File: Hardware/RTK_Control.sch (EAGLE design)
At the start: 294 parts, among them J3 MICRO-SD-PUSH-PUSH-EXT-PIN, J4 Vertical Qwiic Connector, J9 MAGJACK-POE, U1 ESP32-WROVER-IE, U10 POE_PSU-DP990X, U11 MCP6021T, U12 AP7361C-33, U13 MCP6021T, U14 BP2G1+_POWER_SPLITTER, U15 USB251XB, U16 SN74AVC4T774PW, U2 CH340C, U3 XC6222B331MR-G, U4 U-BLOX_ZED-F9P, U5 U-BLOX_NEO-D9S-00B, U6 XC6222B331MR-G, U7 W5500, U8 LARA-R6001, U9 74LVC4066D_QUAD_BILATERAL_SWI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, Y1 25MHz, Y2 24MHz

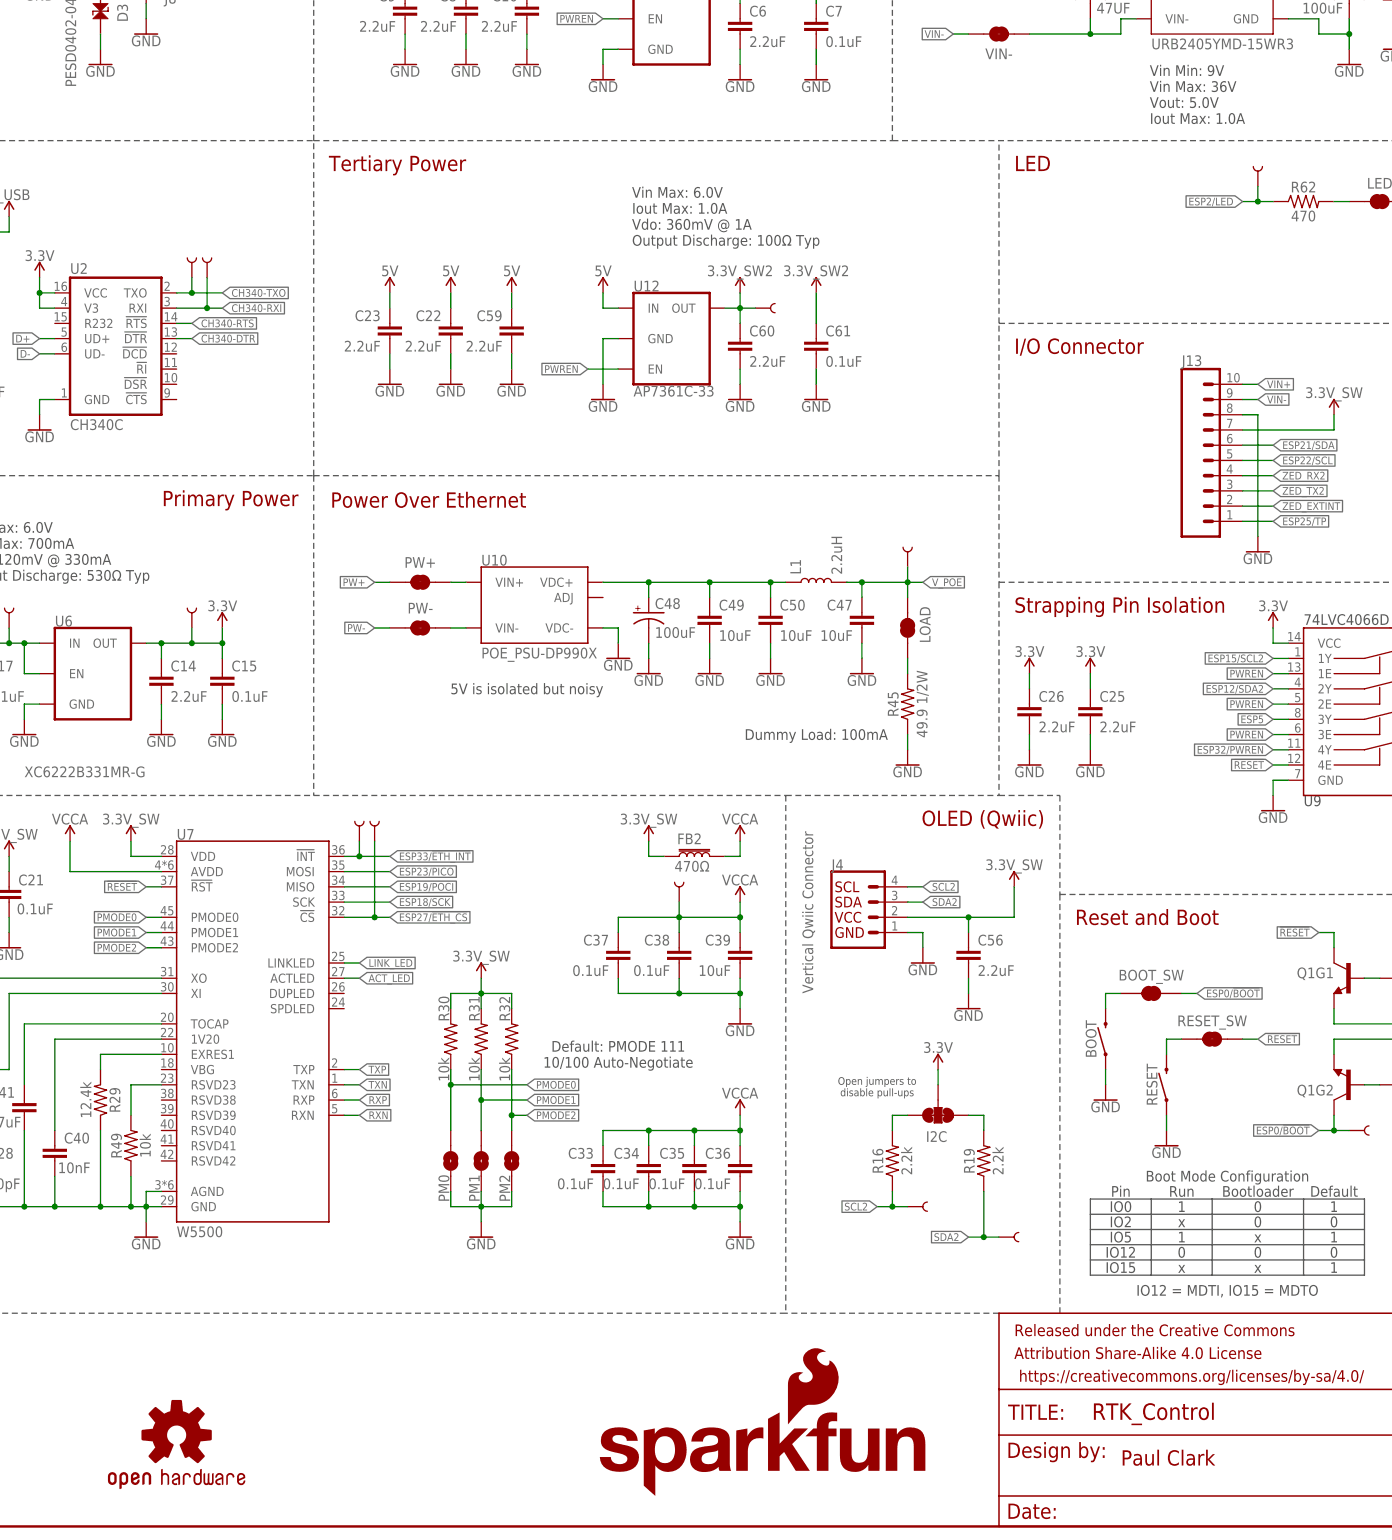
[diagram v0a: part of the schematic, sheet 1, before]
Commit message: Update DC-DC and PoE voltages and currents
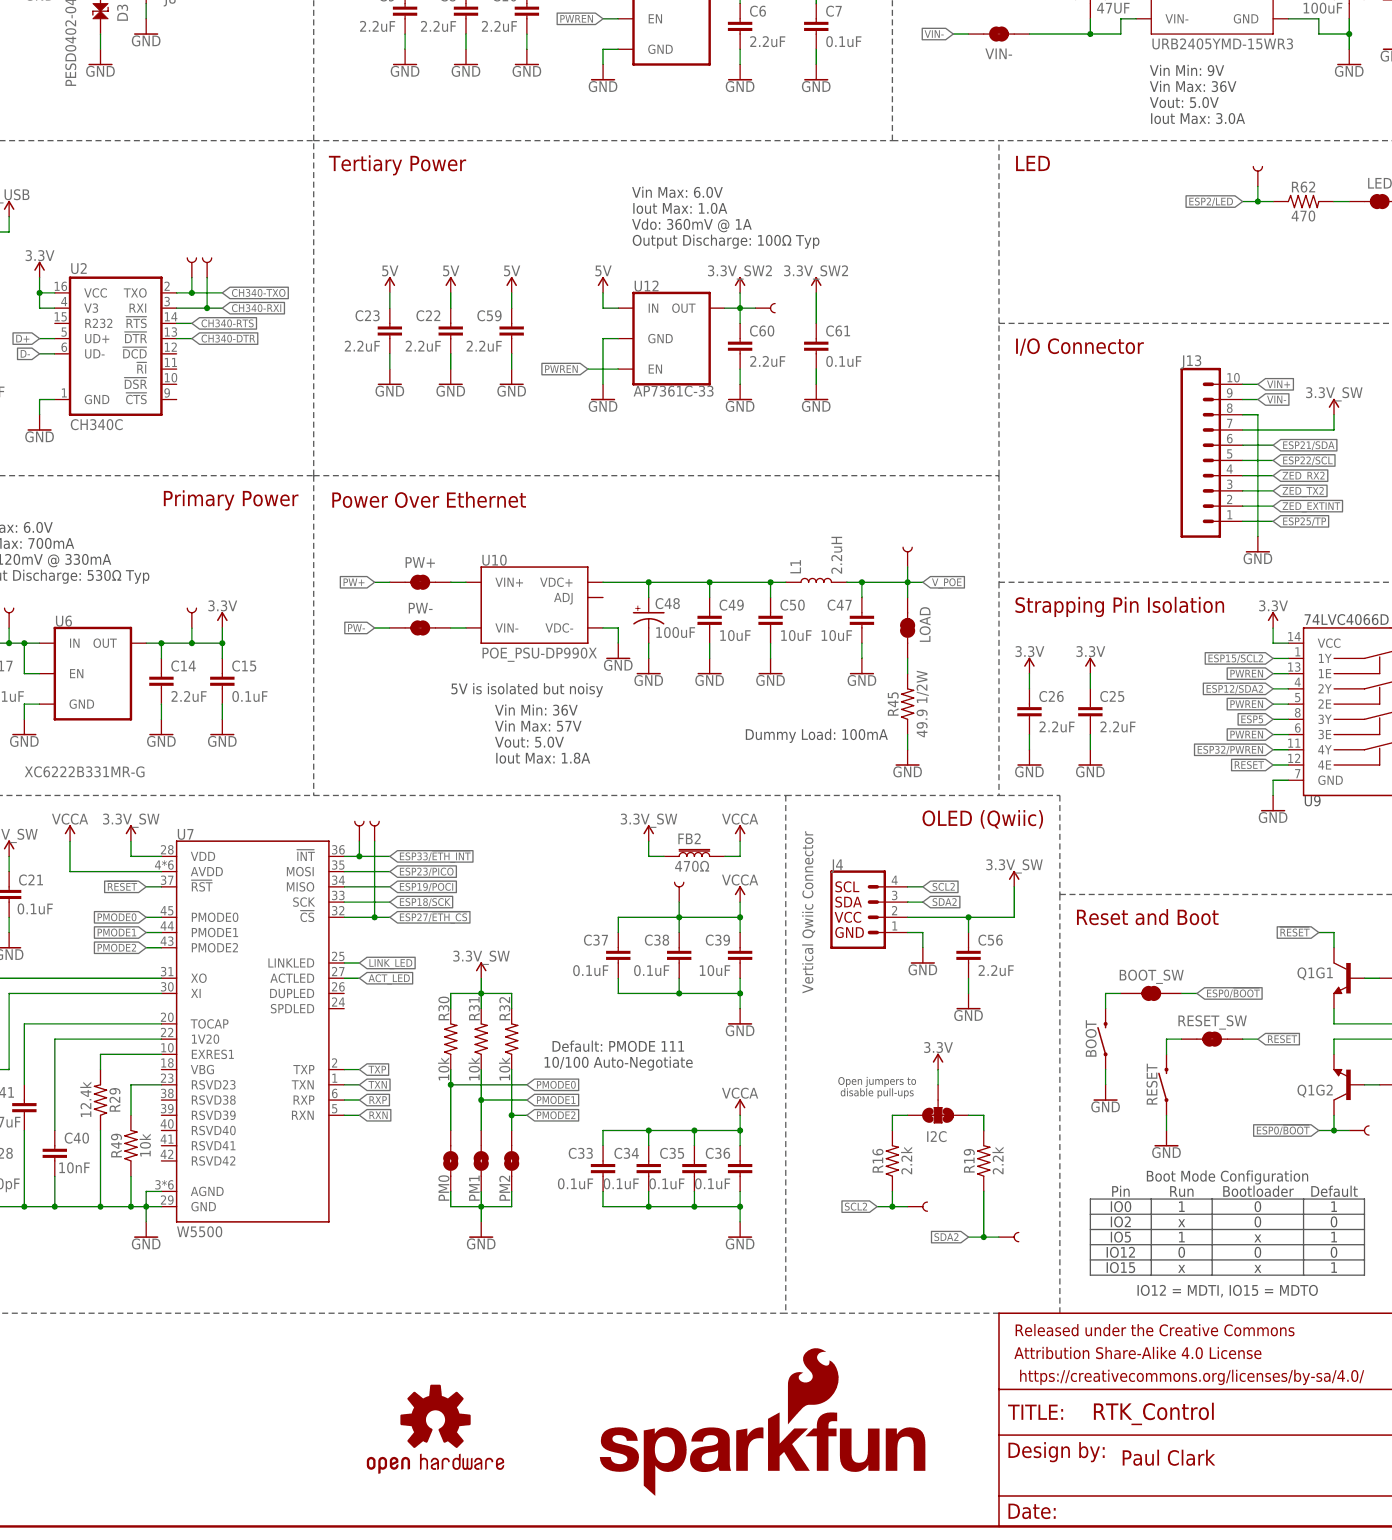
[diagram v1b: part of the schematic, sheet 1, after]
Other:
- note added: "Vin Min: 36V Vin Max: 57V Vout: 5.0V Iout Max: 1.8A"
- note added: "Vin Min: 9V Vin Max: 36V Vout: 5.0V Iout Max: 3.0A"
- note removed: "Vin Min: 9V Vin Max: 36V Vout: 5.0V Iout Max: 1.0A"
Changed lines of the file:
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@@
 Vin Max: 36V
 Vout: 5.0V
-Iout Max: 1.0A</text>
+Iout Max: 3.0A</text>
+<text x="246.126" y="127.254" size="1.778" layer="97" font="vector">Vin Min: 36V
+Vin Max: 57V
+Vout: 5.0V
+Iout Max: 1.8A</text>
 </plain>
 <instances>
@@
 <instance part="5V" gate="G$1" x="165.1" y="149.86" smashed="yes" rot="R90"/>
 <instance part="H4" gate="G$1" x="426.72" y="30.48" smashed="yes"/>
-<instance part="LOGO4" gate="G$1" x="193.04" y="15.24" smashed="yes"/>
+<instance part="LOGO4" gate="G$1" x="236.22" y="17.78" smashed="yes"/>
 <instance part="SUPPLY7" gate="G$1" x="165.1" y="218.44" smashed="yes">
 <attribute name="VALUE" x="165.1" y="221.234" size="1.778" layer="96" align="bottom-center"/>

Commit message: Updates after airwire review
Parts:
- removed R50, R51, R52: 10k, SparkFun-Resistors:10KOHM-0603-1/10W-1%
- added VID1: 10k, SparkFun-Resistors:10KOHM-0603-1/10W-1%
- added VID2: 1k, SparkFun-Resistors:1KOHM-0603-1/10W-1%
- D3: value PESD0402-0402 -> PESD0402
- renumbered U$73 to U17
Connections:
- net DET renamed ESP36/SD_DET
- removed net LARA_RXDO: U16.B2
- removed net LARA_TXDI: U16.B1
- removed net N$37: R50.2, R51.2, U1.IA35
- removed net N$39: R51.1, R52.2
- new net ESP35/VID: U1.IA35, VID1.2, VID2.2
- net 3.3V: now also VID2.1; no longer R52.1
- net ESP13/LARA_TXDI: now also U16.B1
- net ESP14/LARA_RXDO: now also U16.B2
- net GND: now also U16.B4, VID1.1; no longer R50.1
- net VCCIO: now also U16.DIR4
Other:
- note added: "Pin 35 floats at 0.18V approx. 3.3 / 13.3 = 0.82V (0.74 - 0.90) 10 / 30 = 1.1V (0.99 - 1.21) 10 / 20 = 1.65V (1.49 - 1.82) 20 / 30 = 2.2V (1.98 - 2.42) 10 / 13.3 = 2.48V (2.23 - 2.73) 10 / 11 = 3.00V (2.70 - 3.30)"
- note added: "Product Identifier"
- note added: "RTK Product Voltage IDs: Surveyor: Express: Reference Station: Facet: Facet L-Band: Express Plus: Control:"
- moved on the sheet: C11, C13, C18, C19, C20, D1, D3, ESP32_RF, FB1, GNSS_RF, J8, R11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

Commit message: Ready for routing
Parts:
- added ESP5: TEST-POINTPOGO_PTH, SparkFun-Connectors:TEST-POINTPOGO_PTH
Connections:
- new net N$37: ESP5.1, U9.3Z
- net D+_LARA: now also R10.1; no longer R9.1
- net D-_LARA: now also R9.1; no longer R10.1
- net GND: no longer U16.B4
- net VCCIO: now also U16.A4
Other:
- moved on the sheet: C19
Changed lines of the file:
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@@
 <part name="SDA" library="SparkFun-Connectors" deviceset="TEST-POINT" device="POGO_PTH" value="TEST-POINTPOGO_PTH"/>
 <part name="SUPPLY63" library="SparkFun-PowerSymbols" deviceset="3.3V_SW" device=""/>
+<part name="ESP5" library="SparkFun-Connectors" deviceset="TEST-POINT" device="POGO_PTH" value="TEST-POINTPOGO_PTH"/>
+<part name="GND49" library="SparkFun-PowerSymbols" deviceset="GND" device=""/>
 </parts>
 <sheets>
@@
 <attribute name="VALUE" x="20.32" y="152.146" size="1.778" layer="96" align="top-center"/>
 </instance>
-<instance part="C19" gate="G$1" x="7.62" y="137.16" smashed="yes">
-<attribute name="NAME" x="9.144" y="140.081" size="1.778" layer="95" font="vector"/>
-<attribute name="VALUE" x="9.144" y="135.001" size="1.778" layer="96" font="vector"/>
+<instance part="C19" gate="G$1" x="7.62" y="134.62" smashed="yes">
+<attribute name="NAME" x="9.144" y="137.541" size="1.778" layer="95" font="vector"/>
+<attribute name="VALUE" x="9.144" y="132.461" size="1.778" layer="96" font="vector"/>
 </instance>
 <instance part="GND38" gate="1" x="7.62" y="127" smashed="yes">
 <attribute name="VALUE" x="7.62" y="126.746" size="1.778" layer="96" align="top-center"/>
 </instance>
-<instance part="SUPPLY27" gate="G$1" x="7.62" y="144.78" smashed="yes">
-<attribute name="VALUE" x="7.62" y="147.574" size="1.778" layer="96" align="bottom-center"/>
+<instance part="SUPPLY27" gate="G$1" x="7.62" y="142.24" smashed="yes">
+<attribute name="VALUE" x="7.62" y="145.034" size="1.778" layer="96" align="bottom-center"/>
 </instance>
 <instance part="SUPPLY28" gate="G$1" x="7.62" y="167.64" smashed="yes">
@@
 <instance part="SD_CS" gate="G$1" x="55.88" y="152.4" smashed="yes" rot="R90"/>
 <instance part="SCK" gate="G$1" x="53.34" y="144.78" smashed="yes" rot="R90"/>
-<instance part="GND" gate="G$1" x="10.16" y="132.08" smashed="yes"/>
+<instance part="GND" gate="G$1" x="134.62" y="137.16" smashed="yes" rot="R90"/>
 <instance part="RESET_SW" gate="G$1" x="365.76" y="81.28" smashed="yes" rot="MR0">
 <attribute name="NAME" x="365.76" y="84.328" size="1.778" layer="95" font="vector" rot="MR0" align="center"/>
@@
 <attribute name="VALUE" x="355.6" y="246.38" size="1.778" layer="96" font="vector"/>
 </instance>
+<instance part="ESP5" gate="G$1" x="411.48" y="134.62" smashed="yes">
+<attribute name="NAME" x="416.56" y="134.62" size="1.778" layer="95" font="vector"/>
+</instance>
+<instance part="GND49" gate="1" x="134.62" y="132.08" smashed="yes">
+<attribute name="VALUE" x="134.62" y="131.826" size="1.778" layer="96" align="top-center"/>
+</instance>
 </instances>
 <busses>
@@
 <pinref part="C19" gate="G$1" pin="2"/>
 <wire x1="7.62" y1="129.54" x2="7.62" y2="132.08" width="0.1524" layer="91"/>
-<pinref part="GND" gate="G$1" pin="1"/>
-<wire x1="7.62" y1="132.08" x2="7.62" y2="134.62" width="0.1524" layer="91"/>
-<wire x1="10.16" y1="132.08" x2="7.62" y2="132.08" width="0.1524" layer="91"/>
-<junction x="7.62" y="132.08"/>
 </segment>
 <segment>
@@
 <wire x1="419.1" y1="248.92" x2="419.1" y2="251.46" width="0.1524" layer="91"/>
 </segment>
+<segment>
+<pinref part="GND49" gate="1" pin="GND"/>
+<pinref part="GND" gate="G$1" pin="1"/>
+<wire x1="134.62" y1="134.62" x2="134.62" y2="137.16" width="0.1524" layer="91"/>
+</segment>
 </net>
 <net name="3.3V" class="0">
@@
 <pinref part="C19" gate="G$1" pin="1"/>
 <pinref part="SUPPLY27" gate="G$1" pin="3.3V_SW"/>
-<wire x1="7.62" y1="142.24" x2="7.62" y2="144.78" width="0.1524" layer="91"/>
+<wire x1="7.62" y1="139.7" x2="7.62" y2="142.24" width="0.1524" layer="91"/>
 </segment>
 <segment>
@@
 </segment>
 </net>
+<net name="N$37" class="0">
+<segment>
+<pinref part="U9" gate="G$1" pin="3Z"/>
+<pinref part="ESP5" gate="G$1" pin="1"/>
+<wire x1="408.94" y1="134.62" x2="411.48" y2="134.62" width="0.1524" layer="91"/>
+</segment>
+</net>
 </nets>
 </sheet>
@@
 <wire x1="254" y1="157.48" x2="254" y2="279.4" width="0.1524" layer="97" style="longdash"/>
 <text x="326.39" y="187.96" size="1.778" layer="97" font="vector">90Ω</text>
-<text x="279.4" y="81.28" size="1.778" layer="97" align="center">7-bit unshifted I²C address: 0x2C</text>
+<text x="279.4" y="81.28" size="1.778" layer="97" font="vector" align="center">7-bit unshifted I²C address: 0x2C</text>
 <text x="279.4" y="76.2" size="1.27" layer="97" font="vector" align="center">Any USB2512*, USB2513, or USB2514 can be used
 USB2513 or higher required for NEO variant</text>
@@
 <wire x1="307.34" y1="236.22" x2="309.88" y2="236.22" width="0.1524" layer="91"/>
 <junction x="309.88" y="236.22"/>
-<pinref part="U16" gate="G$1" pin="B4"/>
-<wire x1="307.34" y1="241.3" x2="309.88" y2="241.3" width="0.1524" layer="91"/>
-<wire x1="309.88" y1="241.3" x2="309.88" y2="238.76" width="0.1524" layer="91"/>
-<junction x="309.88" y="238.76"/>
 </segment>
 <segment>
@@
 <net name="D+_LARA" class="0">
 <segment>
-<pinref part="R9" gate="G$1" pin="1"/>
-<wire x1="332.74" y1="190.5" x2="325.12" y2="190.5" width="0.1524" layer="91"/>
-<label x="325.12" y="190.5" size="1.27" layer="95" font="vector" rot="R180" xref="yes"/>
-</segment>
-<segment>
 <pinref part="U15" gate="U1" pin="USBDP_DN1"/>
 <wire x1="299.72" y1="142.24" x2="302.26" y2="142.24" width="0.1524" layer="91"/>
 <label x="302.26" y="142.24" size="1.27" layer="95" xref="yes"/>
 </segment>
-</net>
-<net name="D-_LARA" class="0">
 <segment>
 <pinref part="R10" gate="G$1" pin="1"/>
@@
 <label x="325.12" y="187.96" size="1.27" layer="95" font="vector" rot="R180" xref="yes"/>
 </segment>
+</net>
+<net name="D-_LARA" class="0">
 <segment>
 <pinref part="U15" gate="U1" pin="USBDM_DN1"/>
@@
 <label x="302.26" y="144.78" size="1.27" layer="95" xref="yes"/>
 </segment>
+<segment>
+<pinref part="R9" gate="G$1" pin="1"/>
+<wire x1="332.74" y1="190.5" x2="325.12" y2="190.5" width="0.1524" layer="91"/>
+<label x="325.12" y="190.5" size="1.27" layer="95" font="vector" rot="R180" xref="yes"/>
+</segment>
 </net>
 <net name="USB_!RESET" class="0">
@@
 <pinref part="U16" gate="G$1" pin="DIR3"/>
 <wire x1="284.48" y1="238.76" x2="279.4" y2="238.76" width="0.1524" layer="91"/>
-<wire x1="279.4" y1="238.76" x2="279.4" y2="251.46" width="0.1524" layer="91"/>
+<wire x1="279.4" y1="238.76" x2="279.4" y2="241.3" width="0.1524" layer="91"/>
 <junction x="279.4" y="251.46"/>
 <pinref part="U16" gate="G$1" pin="DIR4"/>
+<wire x1="279.4" y1="241.3" x2="279.4" y2="251.46" width="0.1524" layer="91"/>
 <wire x1="284.48" y1="236.22" x2="279.4" y2="236.22" width="0.1524" layer="91"/>
 <wire x1="279.4" y1="236.22" x2="279.4" y2="238.76" width="0.1524" layer="91"/>
 <junction x="279.4" y="238.76"/>
+<pinref part="U16" gate="G$1" pin="A4"/>
+<wire x1="284.48" y1="241.3" x2="279.4" y2="241.3" width="0.1524" layer="91"/>
+<junction x="279.4" y="241.3"/>
 </segment>
 </net>

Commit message: Partially routed
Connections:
- net N$22 renamed VIN1+
- net N$66 renamed VIN1-
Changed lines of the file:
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@@
 </segment>
 </net>
-<net name="N$22" class="0">
+<net name="VIN1+" class="0">
 <segment>
 <pinref part="VIN+" gate="JP1" pin="1"/>
@@
 </segment>
 </net>
-<net name="N$66" class="0">
+<net name="VIN1-" class="0">
 <segment>
 <pinref part="U17" gate="U1" pin="VIN-"/>
